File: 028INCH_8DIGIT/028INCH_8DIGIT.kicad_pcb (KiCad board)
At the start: 2 copper layers, 43.8 x 21 mm, 10 parts, among them J1 Conn_01x04_Female, J2 Conn_01x04_Male, U1 JM-S03651BH, U2 TM1637

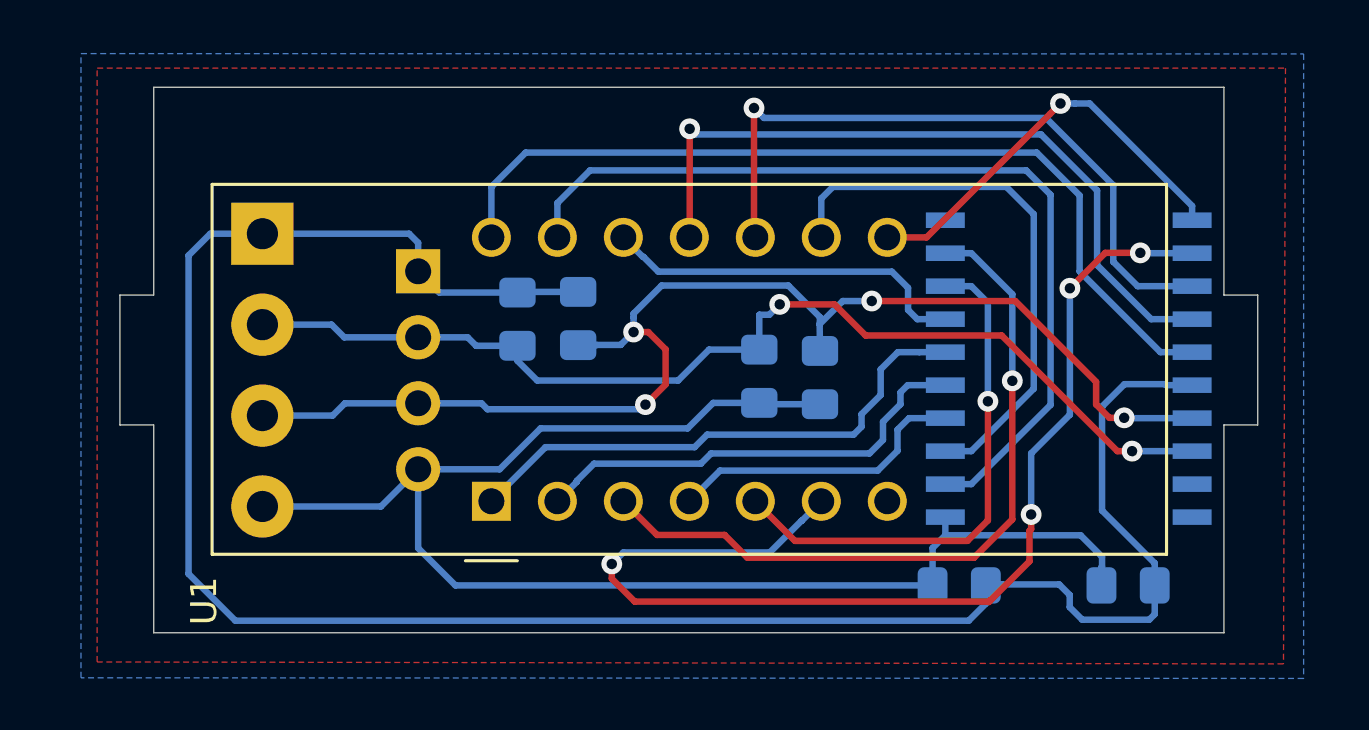
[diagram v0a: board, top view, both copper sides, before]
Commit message: start element placing
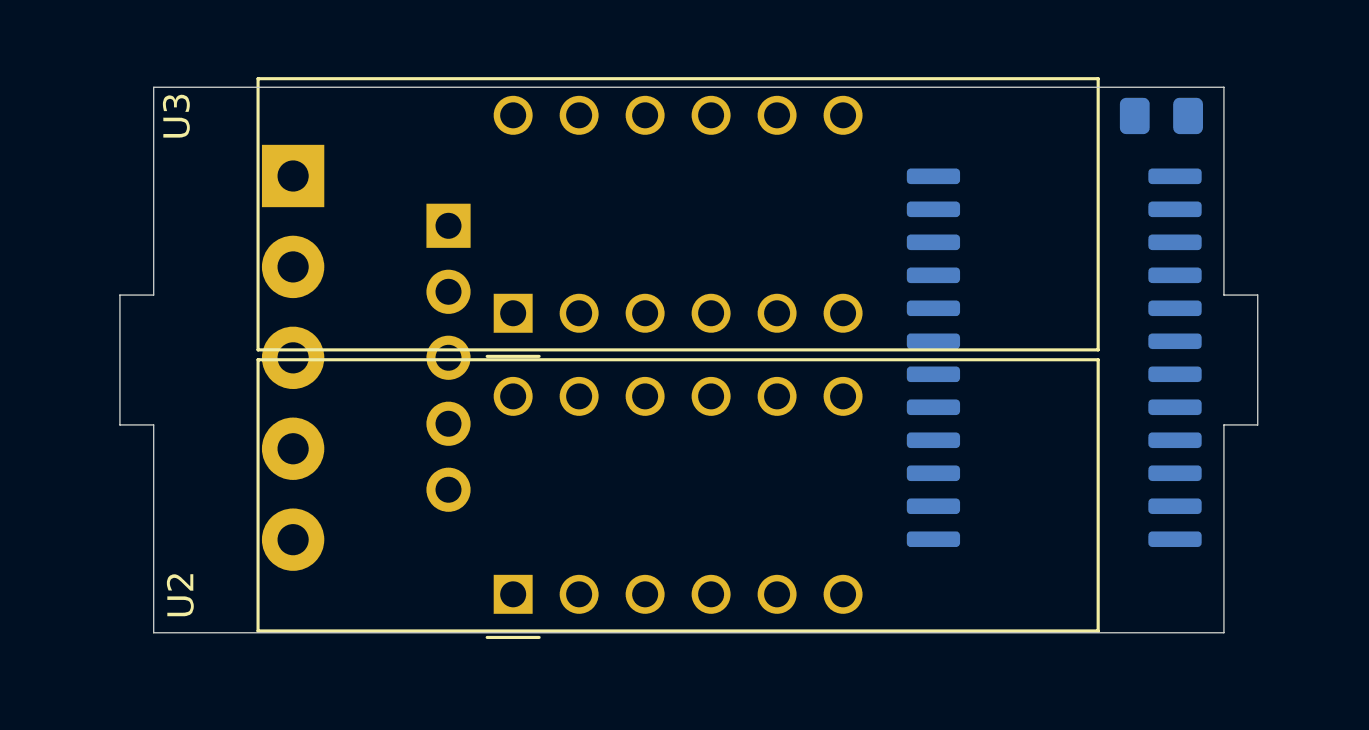
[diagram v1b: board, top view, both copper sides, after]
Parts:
- removed C1: 10uF, Capacitor_SMD:C_0805_2012Metric_Pad1.15x1.40mm_HandSolder
- removed C2: 100nF, Capacitor_SMD:C_0805_2012Metric_Pad1.15x1.40mm_HandSolder
- removed C3, C4: 100pF, Capacitor_SMD:C_0805_2012Metric_Pad1.15x1.40mm_HandSolder
- removed R2: 10k, Resistor_SMD:R_0805_2012Metric_Pad1.15x1.40mm_HandSolder
- added U3: CC56-12CGKWA, XLITX:2841AS, F.Cu at (115.1, 108.7)
- J1: value Conn_01x04_Female -> Conn_01x05_Female; footprint TerminalBlock_4Ucon:TerminalBlock_4Ucon_1x04_P3.50mm_Horizontal -> TerminalBlock_4Ucon:TerminalBlock_4Ucon_1x05_P3.50mm_Horizontal
- J2: value Conn_01x04_Male -> Conn_01x05_Male; footprint Connector_PinHeader_2.54mm:PinHeader_1x04_P2.54mm_Vertical -> Connector_PinHeader_2.54mm:PinHeader_1x05_P2.54mm_Vertical
- U1: value JM-S03651BH -> MAX7219; footprint JINGMEI:JM-S03651BH -> Package_SO:SOIC-24W_7.5x15.4mm_P1.27mm; moved to B.Cu
- U2: value TM1637 -> CC56-12CGKWA; footprint Package_SO:SO-20_12.8x7.5mm_P1.27mm -> XLITX:2841AS; moved to F.Cu
- moved R1 26.0 mm to (140.1, 101.1), turned to 0 degrees
- moved U2 23.1 mm to (115.1, 119.5), turned to 90 degrees
- moved U1 22.4 mm to (136.0, 110.4), turned to 0 degrees
- moved J1 2.52 mm to (106.7, 103.4)
- moved J2 2.11 mm to (112.6, 105.3)
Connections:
- J1 pad 1: Net-(C1-Pad1) -> Net-(J1-Pad1)
- J1 pad 2: Net-(C3-Pad1) -> Net-(J1-Pad2)
- J1 pad 3: Net-(C4-Pad1) -> Net-(J1-Pad3)
- J1 pad 4: Net-(C1-Pad2) -> Net-(J1-Pad4)
- J2 pad 1: Net-(C1-Pad1) -> Net-(J1-Pad1)
- J2 pad 2: Net-(C3-Pad1) -> Net-(J1-Pad2)
- J2 pad 3: Net-(C4-Pad1) -> Net-(J1-Pad3)
- J2 pad 4: Net-(C1-Pad2) -> Net-(J1-Pad4)
- R1 pad 1: Net-(C1-Pad1) -> Net-(J1-Pad1)
- R1 pad 2: Net-(C3-Pad1) -> Net-(R1-Pad2)
- U1 pad 1: Net-(U1-Pad1) -> Net-(J1-Pad4)
- U1 pad 12: Net-(U1-Pad12) -> Net-(J1-Pad2)
- U1 pad 13: Net-(U1-Pad13) -> Net-(J1-Pad3)
- U1 pad 4: Net-(U1-Pad4) -> Net-(J1-Pad5)
- U1 pad 9: Net-(U1-Pad9) -> Net-(J1-Pad5)
- U2 pad 1: Net-(C1-Pad2) -> Net-(U1-Pad21)
- U2 pad 10: Net-(U2-Pad10) -> Net-(U1-Pad15)
- U2 pad 11: Net-(U1-Pad8) -> Net-(U1-Pad14)
- U2 pad 12: Net-(U1-Pad6) -> Net-(U1-Pad3)
- U2 pad 2: Net-(U1-Pad13) -> Net-(U1-Pad23)
- U2 pad 3: Net-(U1-Pad9) -> Net-(U1-Pad22)
- U2 pad 4: Net-(U1-Pad4) -> Net-(U1-Pad20)
- U2 pad 5: Net-(U1-Pad2) -> Net-(U1-Pad17)
- U2 pad 6: Net-(U1-Pad1) -> Net-(U1-Pad8)
- U2 pad 7: Net-(U1-Pad12) -> Net-(U1-Pad16)
- U2 pad 9: Net-(U1-Pad3) -> Net-(U1-Pad10)
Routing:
- net Net-(C1-Pad1): track 81.7 -> 0.00 mm
- net Net-(C1-Pad2): track 56.9 -> 0.00 mm
- net Net-(C4-Pad1): track 48.6 -> 0.00 mm, vias 4 -> 0
- net Net-(U1-Pad6): track 43.3 -> 0.00 mm, vias 4 -> 0
- net Net-(C3-Pad1): track 41.4 -> 0.00 mm, vias 2 -> 0
- net Net-(U1-Pad13): track 34.6 -> 0.00 mm
- net Net-(U1-Pad14): track 34.4 -> 0.00 mm
- net Net-(U1-Pad3): track 28.4 -> 0.00 mm, vias 1 -> 0
- net Net-(U1-Pad11): track 28.2 -> 0.00 mm, vias 1 -> 0
- net Net-(U1-Pad10): track 26.4 -> 0.00 mm, vias 1 -> 0
- net Net-(U1-Pad9): track 21.4 -> 0.00 mm
- net Net-(U1-Pad1): track 20.7 -> 0.00 mm
- net Net-(U1-Pad5): track 20.2 -> 0.00 mm, vias 1 -> 0
- net Net-(U1-Pad2): track 17.5 -> 0.00 mm
- net Net-(U1-Pad8): track 16.1 -> 0.00 mm, vias 1 -> 0
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- removed copper zone on B.Cu, net Net-(C1-Pad2)
- removed copper zone on F.Cu, net Net-(C1-Pad2)
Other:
- board text added: "028_8DIG"
- board text removed: "+ C D -"
- board text removed: "036_5DIG"

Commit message: all elements placed
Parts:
- moved R1 3.40 mm to (136.7, 101.3)
- moved U3 0.40 mm to (115.1, 109.1)
- moved J2 0.09 mm to (112.6, 105.4)
- moved J1 0.08 mm to (106.7, 103.5)
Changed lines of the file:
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@@
   (general
     (thickness 1.6)
-    (drawings 13)
+    (drawings 14)
     (tracks 0)
     (zones 0)
@@
   )
   (module XLITX:2841AS (layer F.Cu)
-    (at 115.1382 108.7 90)
+    (at 115.1382 109.1 90)
     (descr "4 digit 7 segment red LED, http://xlitx.com/datasheet/2841AS.pdf")
     (tags "4 digit 7 segment red LED")
@@
   )
   (module XLITX:2841AS (layer F.Cu)
-    (at 115.1382 119.5197 90)
+    (at 115.1382 119.52 90)
     (descr "4 digit 7 segment red LED, http://xlitx.com/datasheet/2841AS.pdf")
     (tags "4 digit 7 segment red LED")
@@
   )
   (module Resistor_SMD:R_0805_2012Metric_Pad1.15x1.40mm_HandSolder (layer B.Cu)
-    (at 140.0937 101.1047)
+    (at 136.7028 101.2825)
     (descr "Resistor SMD 0805 (2012 Metric), square (rectangular) end terminal, IPC_7351 nominal with elongated pad for handsoldering. (Body size source: https://docs.google.com/spreadsheets/d/1BsfQQcO9C6DZCsRaXUlFlo91Tg2WpOkGARC1WS5S8t0/edit?usp=sharing), generated with kicad-footprint-generator")
     (tags "resistor handsolder")
@@
   )
   (module Connector_PinHeader_2.54mm:PinHeader_1x05_P2.54mm_Vertical (layer B.Cu)
-    (at 112.649 105.3338 180)
+    (at 112.649 105.42 180)
     (descr "Through hole straight pin header, 1x05, 2.54mm pitch, single row")
     (tags "Through hole pin header THT 1x05 2.54mm single row")
@@
   )
   (module TerminalBlock_4Ucon:TerminalBlock_4Ucon_1x05_P3.50mm_Horizontal (layer B.Cu)
-    (at 106.6673 103.4161 270)
+    (at 106.6673 103.5 270)
     (descr "Terminal Block 4Ucon ItemNo. 20223, 5 pins, pitch 3.5mm, size 18.2x7mm^2, drill diamater 1.2mm, pad diameter 2.4mm, see http://www.4uconnector.com/online/object/4udrawing/20223.pdf, script-generated using https://github.com/pointhi/kicad-footprint-generator/scripts/TerminalBlock_4Ucon")
     (tags "THT Terminal Block 4Ucon ItemNo. 20223 pitch 3.5mm size 18.2x7mm^2 drill 1.2mm pad 2.4mm")
@@
     )
   )
+  (gr_line (start 100 110.5) (end 143.8 110.5) (layer F.SilkS) (width 0.12))
   (gr_text 028_8DIG (at 107.2388 101.4349) (layer B.SilkS)
     (effects (font (size 1 1) (thickness 0.15)) (justify mirror))

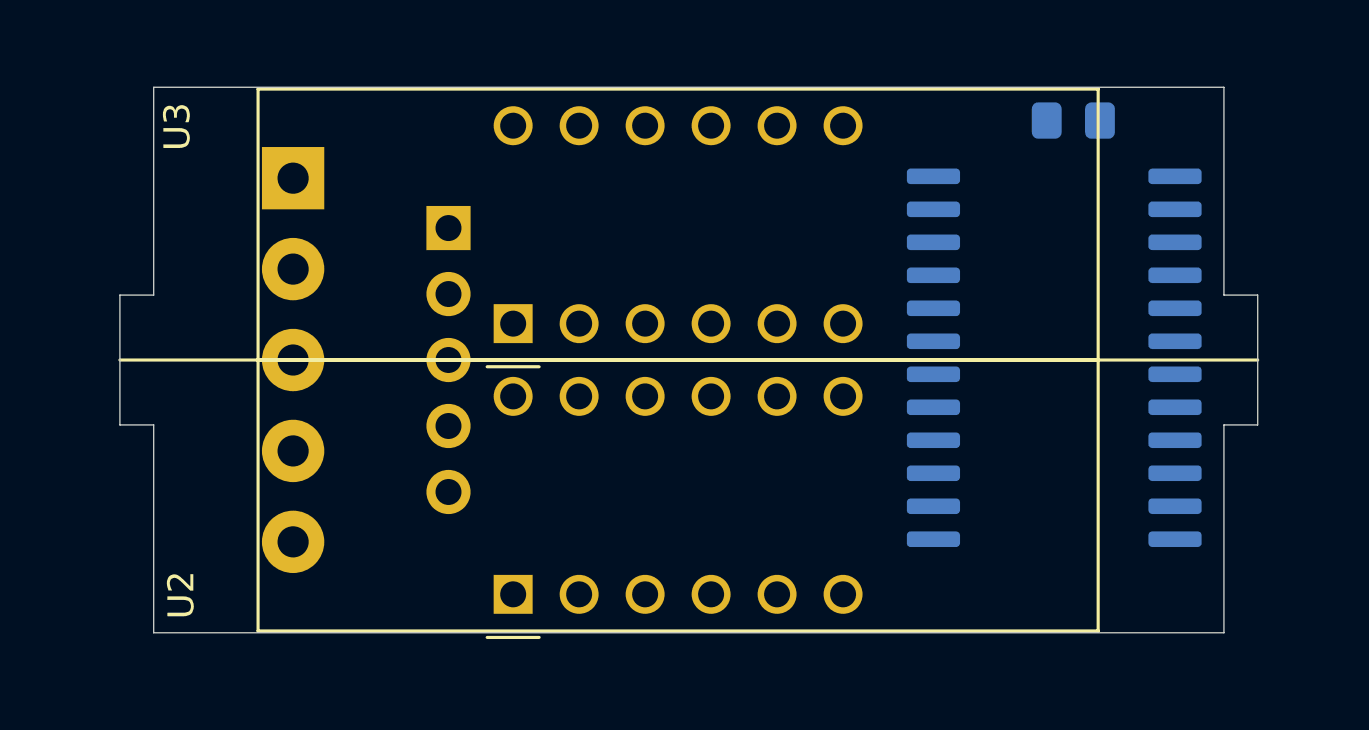
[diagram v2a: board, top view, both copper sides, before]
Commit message: all traces routed
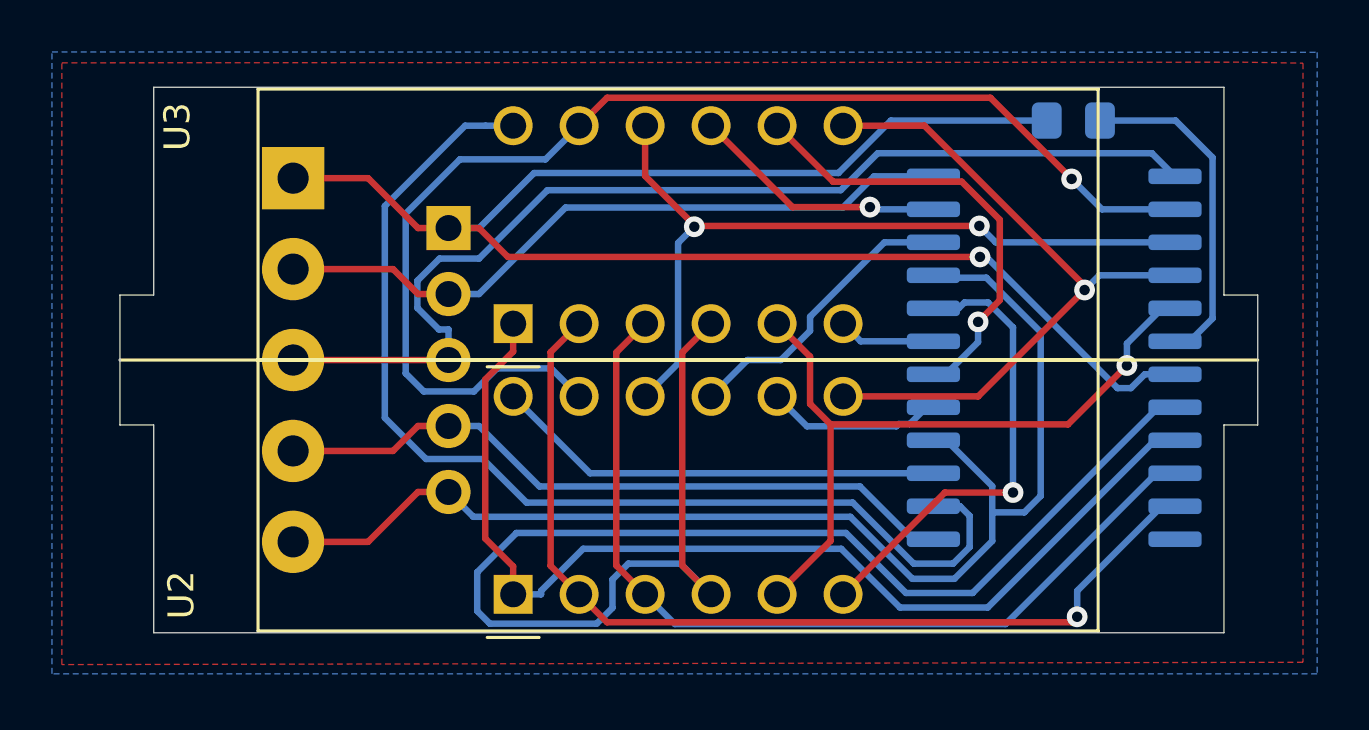
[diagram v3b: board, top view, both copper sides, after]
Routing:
- net Net-(J1-Pad1): track 0.00 -> 62.3 mm, vias 0 -> 1
- net Net-(U1-Pad20): track 0.00 -> 55.5 mm
- net Net-(J1-Pad5): track 0.00 -> 48.3 mm
- net Net-(U1-Pad14): track 0.00 -> 47.2 mm, vias 0 -> 1
- net Net-(U1-Pad2): track 0.00 -> 42.2 mm
- net Net-(J1-Pad3): track 0.00 -> 41.3 mm
- net Net-(U1-Pad21): track 0.00 -> 41.2 mm
- net Net-(U1-Pad23): track 0.00 -> 37.1 mm, vias 0 -> 1
- net Net-(U1-Pad22): track 0.00 -> 34.6 mm
- net Net-(U1-Pad15): track 0.00 -> 30.7 mm, vias 0 -> 2
- net Net-(U1-Pad17): track 0.00 -> 27.7 mm, vias 0 -> 1
- net Net-(J1-Pad2): track 0.00 -> 26.9 mm
- net Net-(J1-Pad4): track 0.00 -> 26.9 mm
- net Net-(U1-Pad16): track 0.00 -> 26.7 mm, vias 0 -> 1
- net Net-(U1-Pad8): track 0.00 -> 18.1 mm, vias 0 -> 1
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- added copper zone on B.Cu, net Net-(J1-Pad5)
- added copper zone on F.Cu, net Net-(J1-Pad5)
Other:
- board text added: "+ L C D -"
